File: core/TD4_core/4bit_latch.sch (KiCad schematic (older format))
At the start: 4 parts, among them U32 74HC175, U33 74AHC1G08

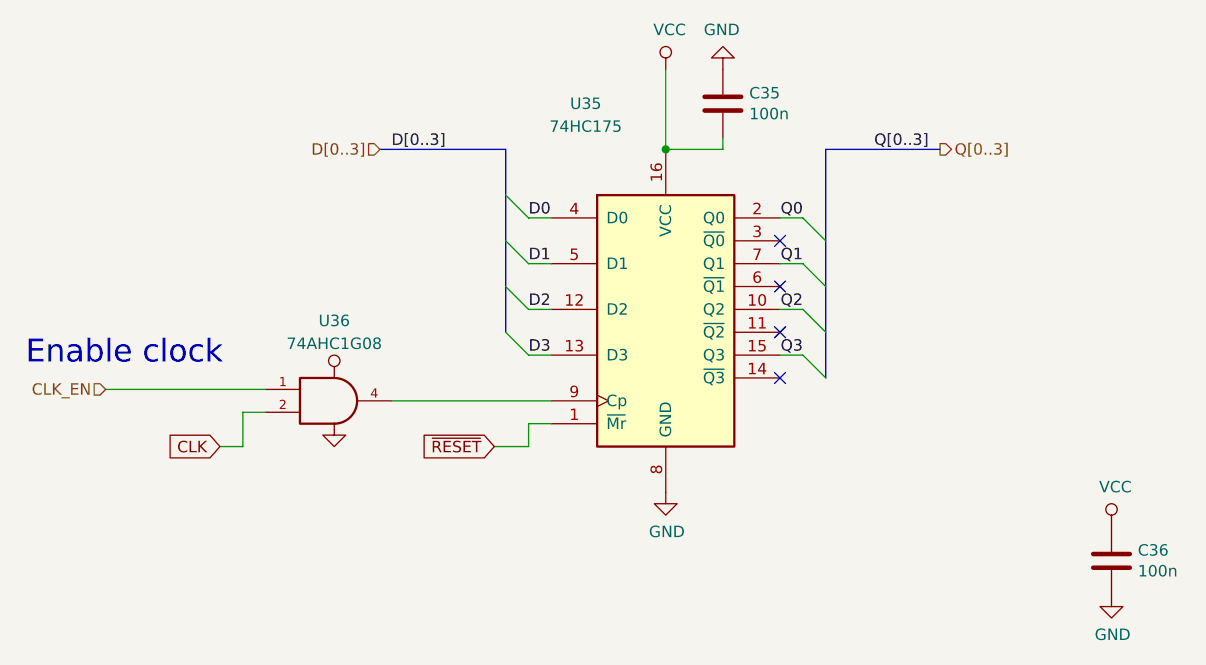
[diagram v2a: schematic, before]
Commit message: Core schematic done. Backplane connector added, including separate .sch file to append.
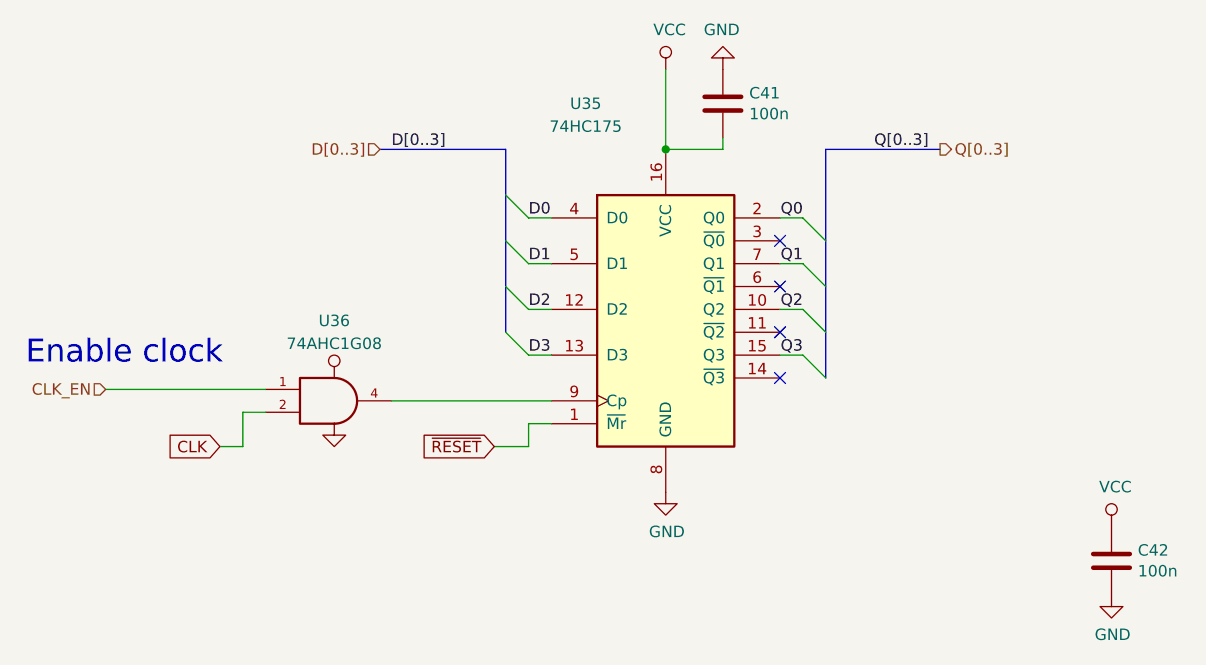
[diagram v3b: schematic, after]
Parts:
- C38: renamed from C32; footprint (none) -> Capacitor_SMD:C_0805_2012Metric
- C39: renamed from C33; footprint (none) -> Capacitor_SMD:C_0805_2012Metric
- U32: footprint (none) -> Package_SO:SOIC-16_3.9x9.9mm_P1.27mm
- U33: footprint (none) -> Package_TO_SOT_SMD:SOT-23-5
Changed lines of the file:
@@
 encoding utf-8
 Sheet 22 23
-Title ""
+Title "TD4 core module"
 Date ""
-Rev ""
+Rev "v1.0"
 Comp ""
 Comment1 ""
@@
 F 0 "U35" H 5500 4550 50  0000 C CNN
 F 1 "74HC175" H 5500 4450 50  0000 C CNN
-F 2 "" H 5850 3650 50  0001 C CNN
+F 2 "Package_SO:SOIC-16_3.9x9.9mm_P1.27mm" H 5850 3650 50  0001 C CNN
 F 3 "http://www.ti.com/lit/gpn/sn74LS175" H 5850 3650 50  0001 C CNN
 	1    5850 3650
@@
 $EndComp
 $Comp
-L Device:C C32
+L Device:C C38
 U 1 1 5C6310BA
 P 6100 2750
-AR Path="/5C63072E/5C6310BA" Ref="C32"  Part="1"
+AR Path="/5C63072E/5C6310BA" Ref="C38"  Part="1"
 AR Path="/5C63A7FA/5C6310BA" Ref="C?"  Part="1"
-AR Path="/5C685283/5C6310BA" Ref="C35"  Part="1"
-F 0 "C35" H 6215 2796 50  0000 L CNN
+AR Path="/5C685283/5C6310BA" Ref="C41"  Part="1"
+F 0 "C41" H 6215 2796 50  0000 L CNN
 F 1 "100n" H 6215 2705 50  0000 L CNN
-F 2 "" H 6138 2600 50  0001 C CNN
+F 2 "Capacitor_SMD:C_0805_2012Metric" H 6138 2600 50  0001 C CNN
 F 3 "~" H 6100 2750 50  0001 C CNN
 	1    6100 2750
@@
 $EndComp
 $Comp
-L power:GND #PWR0107
+L power:GND #PWR0121
 U 1 1 5C631117
 P 6100 2600
-AR Path="/5C63072E/5C631117" Ref="#PWR0107"  Part="1"
+AR Path="/5C63072E/5C631117" Ref="#PWR0121"  Part="1"
 AR Path="/5C63A7FA/5C631117" Ref="#PWR?"  Part="1"
-AR Path="/5C685283/5C631117" Ref="#PWR0116"  Part="1"
-F 0 "#PWR0116" H 6100 2350 50  0001 C CNN
+AR Path="/5C685283/5C631117" Ref="#PWR0130"  Part="1"
+F 0 "#PWR0130" H 6100 2350 50  0001 C CNN
 F 1 "GND" H 6105 2427 50  0000 C CNN
 F 2 "" H 6100 2600 50  0001 C CNN
@@
 $EndComp
 $Comp
-L power:VCC #PWR0106
+L power:VCC #PWR0120
 U 1 1 5C631158
 P 5850 2600
-AR Path="/5C63072E/5C631158" Ref="#PWR0106"  Part="1"
+AR Path="/5C63072E/5C631158" Ref="#PWR0120"  Part="1"
 AR Path="/5C63A7FA/5C631158" Ref="#PWR?"  Part="1"
-AR Path="/5C685283/5C631158" Ref="#PWR0115"  Part="1"
-F 0 "#PWR0115" H 5850 2450 50  0001 C CNN
+AR Path="/5C685283/5C631158" Ref="#PWR0129"  Part="1"
+F 0 "#PWR0129" H 5850 2450 50  0001 C CNN
 F 1 "VCC" H 5867 2773 50  0000 C CNN
 F 2 "" H 5850 2600 50  0001 C CNN
@@
 Connection ~ 5850 2950
 $Comp
-L power:GND #PWR0110
+L power:GND #PWR0124
 U 1 1 5C6319CE
 P 5850 4450
-AR Path="/5C63072E/5C6319CE" Ref="#PWR0110"  Part="1"
+AR Path="/5C63072E/5C6319CE" Ref="#PWR0124"  Part="1"
 AR Path="/5C63A7FA/5C6319CE" Ref="#PWR?"  Part="1"
-AR Path="/5C685283/5C6319CE" Ref="#PWR0119"  Part="1"
-F 0 "#PWR0119" H 5850 4200 50  0001 C CNN
+AR Path="/5C685283/5C6319CE" Ref="#PWR0133"  Part="1"
+F 0 "#PWR0133" H 5850 4200 50  0001 C CNN
 F 1 "GND" H 5855 4277 50  0000 C CNN
 F 2 "" H 5850 4450 50  0001 C CNN
@@
 F 0 "U36" H 4400 4400 50  0000 C CNN
 F 1 "74AHC1G08" H 4400 4300 50  0000 C CNN
-F 2 "" H 4400 4050 50  0001 C CNN
+F 2 "Package_TO_SOT_SMD:SOT-23-5" H 4400 4050 50  0001 C CNN
 F 3 "http://www.ti.com/lit/sg/scyt129e/scyt129e.pdf" H 4400 4050 50  0001 C CNN
 	1    4400 4050
@@
 P 7800 4750
 AR Path="/5C63A7FA/5C6615CC" Ref="C?"  Part="1"
-AR Path="/5C63072E/5C6615CC" Ref="C33"  Part="1"
-AR Path="/5C685283/5C6615CC" Ref="C36"  Part="1"
-F 0 "C36" H 7915 4796 50  0000 L CNN
+AR Path="/5C63072E/5C6615CC" Ref="C39"  Part="1"
+AR Path="/5C685283/5C6615CC" Ref="C42"  Part="1"
+F 0 "C42" H 7915 4796 50  0000 L CNN
 F 1 "100n" H 7915 4705 50  0000 L CNN
-F 2 "" H 7838 4600 50  0001 C CNN
+F 2 "Capacitor_SMD:C_0805_2012Metric" H 7838 4600 50  0001 C CNN
 F 3 "~" H 7800 4750 50  0001 C CNN
 	1    7800 4750
@@
 P 7800 4900
 AR Path="/5C63A7FA/5C66162D" Ref="#PWR?"  Part="1"
-AR Path="/5C63072E/5C66162D" Ref="#PWR0112"  Part="1"
-AR Path="/5C685283/5C66162D" Ref="#PWR0121"  Part="1"
-F 0 "#PWR0121" H 7800 4650 50  0001 C CNN
+AR Path="/5C63072E/5C66162D" Ref="#PWR0126"  Part="1"
+AR Path="/5C685283/5C66162D" Ref="#PWR0135"  Part="1"
+F 0 "#PWR0135" H 7800 4650 50  0001 C CNN
 F 1 "GND" H 7805 4727 50  0000 C CNN
 F 2 "" H 7800 4900 50  0001 C CNN
@@
 P 7800 4600
 AR Path="/5C63A7FA/5C661670" Ref="#PWR?"  Part="1"
-AR Path="/5C63072E/5C661670" Ref="#PWR0111"  Part="1"
-AR Path="/5C685283/5C661670" Ref="#PWR0120"  Part="1"
-F 0 "#PWR0120" H 7800 4450 50  0001 C CNN
+AR Path="/5C63072E/5C661670" Ref="#PWR0125"  Part="1"
+AR Path="/5C685283/5C661670" Ref="#PWR0134"  Part="1"
+F 0 "#PWR0134" H 7800 4450 50  0001 C CNN
 F 1 "VCC" H 7817 4773 50  0000 C CNN
 F 2 "" H 7800 4600 50  0001 C CNN
@@
 	6550 2950 6550 3950
 $Comp
-L power:GND #PWR0118
+L power:GND #PWR0132
 U 1 1 5C75DE80
 P 4400 4150
-AR Path="/5C685283/5C75DE80" Ref="#PWR0118"  Part="1"
-AR Path="/5C63072E/5C75DE80" Ref="#PWR0109"  Part="1"
-F 0 "#PWR0118" H 4400 3900 50  0001 C CNN
+AR Path="/5C685283/5C75DE80" Ref="#PWR0132"  Part="1"
+AR Path="/5C63072E/5C75DE80" Ref="#PWR0123"  Part="1"
+F 0 "#PWR0132" H 4400 3900 50  0001 C CNN
 F 1 "GND" H 4405 3977 50  0001 C CNN
 F 2 "" H 4400 4150 50  0001 C CNN
@@
 $EndComp
 $Comp
-L power:VCC #PWR0117
+L power:VCC #PWR0131
 U 1 1 5C75DEC3
 P 4400 3950
-AR Path="/5C685283/5C75DEC3" Ref="#PWR0117"  Part="1"
-AR Path="/5C63072E/5C75DEC3" Ref="#PWR0108"  Part="1"
-F 0 "#PWR0117" H 4400 3800 50  0001 C CNN
+AR Path="/5C685283/5C75DEC3" Ref="#PWR0131"  Part="1"
+AR Path="/5C63072E/5C75DEC3" Ref="#PWR0122"  Part="1"
+F 0 "#PWR0131" H 4400 3800 50  0001 C CNN
 F 1 "VCC" H 4417 4123 50  0001 C CNN
 F 2 "" H 4400 3950 50  0001 C CNN

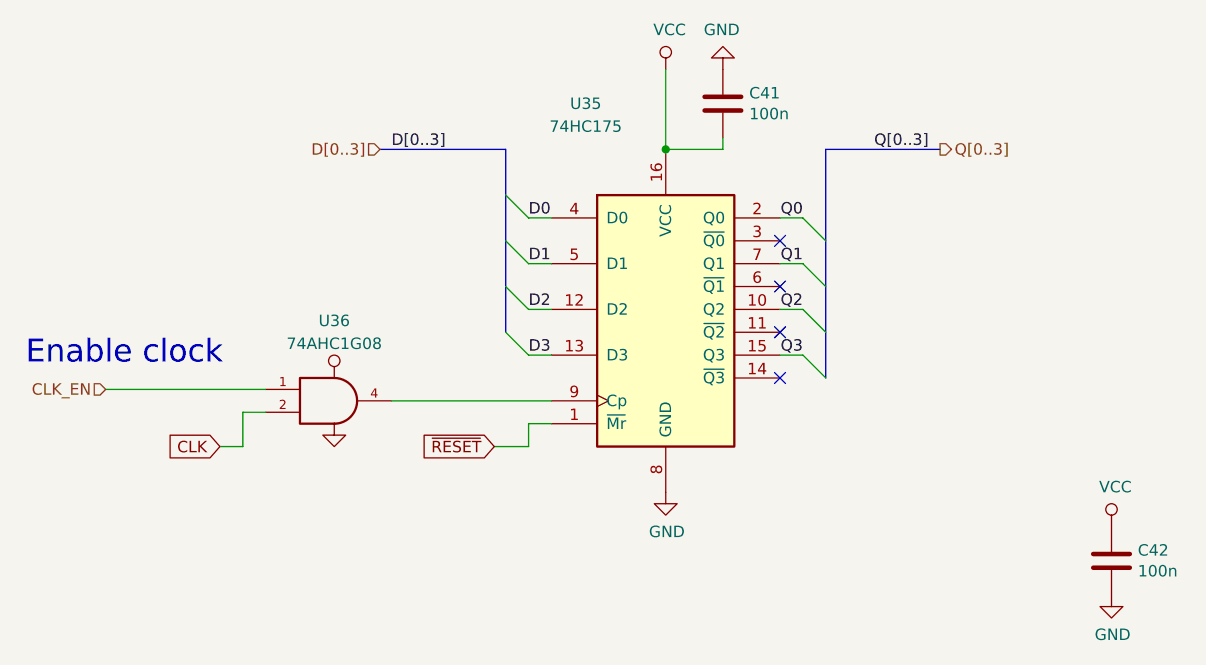
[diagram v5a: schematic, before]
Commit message: Replaced debug headers with vertical ones
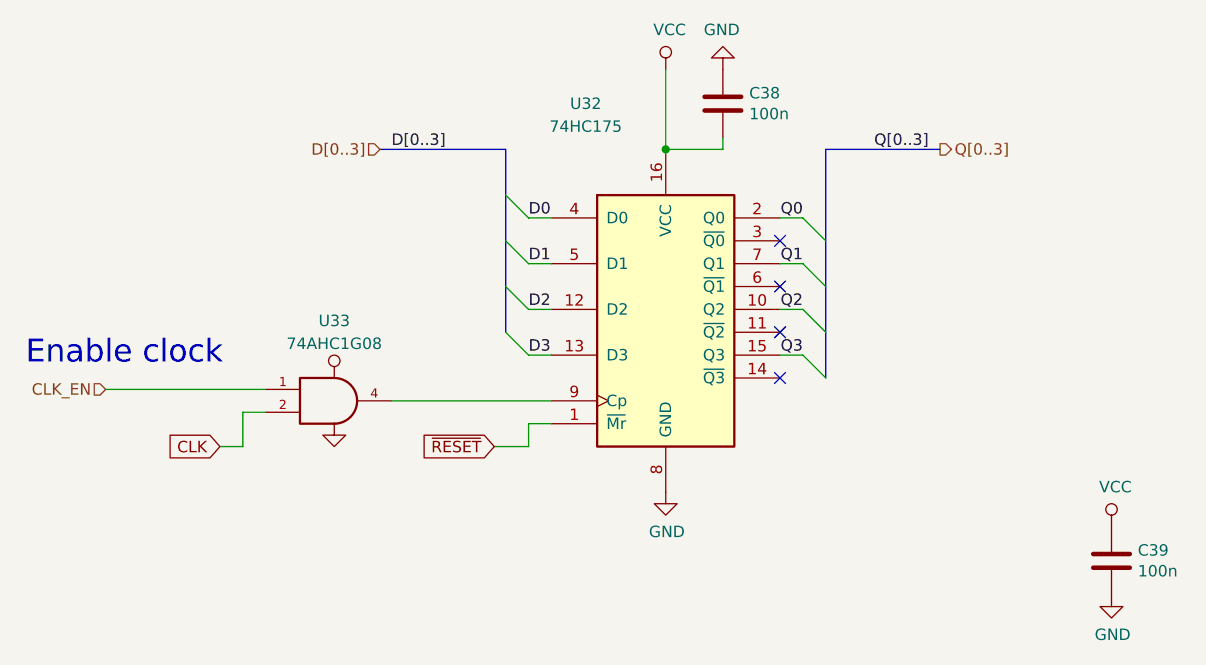
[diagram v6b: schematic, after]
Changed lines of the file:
@@
 AR Path="/5C63A7FA/5C63082C" Ref="U?"  Part="1"
 AR Path="/5C685283/5C63082C" Ref="U35"  Part="1"
-F 0 "U35" H 5500 4550 50  0000 C CNN
+F 0 "U32" H 5500 4550 50  0000 C CNN
 F 1 "74HC175" H 5500 4450 50  0000 C CNN
 F 2 "Package_SO:SOIC-16_3.9x9.9mm_P1.27mm" H 5850 3650 50  0001 C CNN
@@
 AR Path="/5C63A7FA/5C6310BA" Ref="C?"  Part="1"
 AR Path="/5C685283/5C6310BA" Ref="C41"  Part="1"
-F 0 "C41" H 6215 2796 50  0000 L CNN
+F 0 "C38" H 6215 2796 50  0000 L CNN
 F 1 "100n" H 6215 2705 50  0000 L CNN
 F 2 "Capacitor_SMD:C_0805_2012Metric" H 6138 2600 50  0001 C CNN
@@
 AR Path="/5C63A7FA/5C6359C2" Ref="U?"  Part="1"
 AR Path="/5C685283/5C6359C2" Ref="U36"  Part="1"
-F 0 "U36" H 4400 4400 50  0000 C CNN
+F 0 "U33" H 4400 4400 50  0000 C CNN
 F 1 "74AHC1G08" H 4400 4300 50  0000 C CNN
 F 2 "Package_TO_SOT_SMD:SOT-23-5" H 4400 4050 50  0001 C CNN
@@
 AR Path="/5C63072E/5C6615CC" Ref="C39"  Part="1"
 AR Path="/5C685283/5C6615CC" Ref="C42"  Part="1"
-F 0 "C42" H 7915 4796 50  0000 L CNN
+F 0 "C39" H 7915 4796 50  0000 L CNN
 F 1 "100n" H 7915 4705 50  0000 L CNN
 F 2 "Capacitor_SMD:C_0805_2012Metric" H 7838 4600 50  0001 C CNN
